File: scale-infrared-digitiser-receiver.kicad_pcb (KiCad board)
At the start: 4 copper layers, 158 x 6 mm, 59 parts, among them IC0 LM324PT, IC1 LM324PT, IC2 LM324PT, IC3 LM324PT

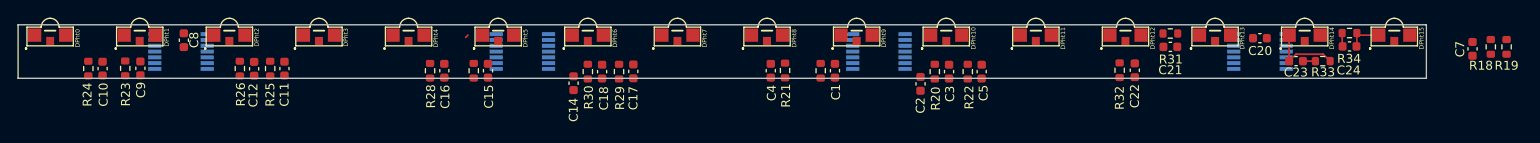
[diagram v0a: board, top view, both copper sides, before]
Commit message: reworking to exclude amplifiers - may need to rollback
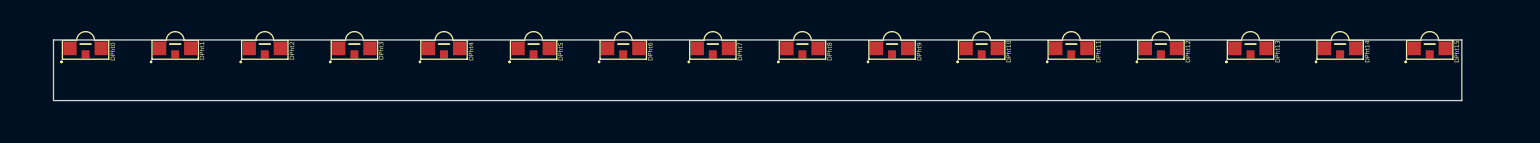
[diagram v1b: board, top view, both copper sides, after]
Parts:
- removed C1, C10, C11, C12, C15, C16, C17, C18, C21, C22, C23, C24, C3, C4, C5, C9: 5.1p, Capacitor_SMD:C_0603_1608Metric
- removed C14, C2, C20, C7, C8: 1u, Capacitor_SMD:C_0603_1608Metric
- removed IC0, IC1, IC2, IC3: LM324PT, Samacsys:SOP65P640X120-14N
- removed R17, R20, R21, R22, R23, R24, R25, R26, R27, R28, R29, R30, R31, R32, R33, R34: 750k, Resistor_SMD:R_0603_1608Metric
- removed R18: 115k, Resistor_SMD:R_0603_1608Metric
- removed R19: 3.57k, Resistor_SMD:R_0603_1608Metric
- moved DPht12 4.25 mm to (194.2, 96.2)
- moved DPht9 4.25 mm to (164.1, 96.2)
- moved DPht1 4.25 mm to (83.7, 96.2)
- moved DPht3 4.25 mm to (103.8, 96.2)
- moved DPht5 4.25 mm to (123.9, 96.2)
- moved DPht0 4.25 mm to (73.6, 96.2)
- moved DPht10 4.25 mm to (174.1, 96.2)
- moved DPht11 4.25 mm to (184.2, 96.2)
- moved DPht13 4.25 mm to (204.3, 96.2)
- moved DPht14 4.25 mm to (214.3, 96.2)
- moved DPht15 4.25 mm to (224.4, 96.2)
- moved DPht2 4.25 mm to (93.7, 96.2)
- moved DPht4 4.25 mm to (113.8, 96.2)
- moved DPht6 4.25 mm to (133.9, 96.2)
- moved DPht7 4.25 mm to (144.0, 96.2)
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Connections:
- DPht0 pad 1: Net-(DPht0-K) -> /PHT_DAT_0
- DPht1 pad 1: Net-(DPht1-K) -> /PHT_DAT_1
- DPht10 pad 1: Net-(DPht10-K) -> /PHT_DAT_10
- DPht11 pad 1: Net-(DPht11-K) -> /PHT_DAT_11
- DPht12 pad 1: Net-(DPht12-K) -> /PHT_DAT_12
- DPht13 pad 1: Net-(DPht13-K) -> /PHT_DAT_13
- DPht14 pad 1: Net-(DPht14-K) -> /PHT_DAT_14
- DPht15 pad 1: Net-(DPht15-K) -> /PHT_DAT_15
- DPht2 pad 1: Net-(DPht2-K) -> /PHT_DAT_2
- DPht3 pad 1: Net-(DPht3-K) -> /PHT_DAT_3
- DPht4 pad 1: Net-(DPht4-K) -> /PHT_DAT_4
- DPht5 pad 1: Net-(DPht5-K) -> /PHT_DAT_5
- DPht6 pad 1: Net-(DPht6-K) -> /PHT_DAT_6
- DPht7 pad 1: Net-(DPht7-K) -> /PHT_DAT_7
- DPht8 pad 1: Net-(DPht8-K) -> /PHT_DAT_8
- DPht9 pad 1: Net-(DPht9-K) -> /PHT_DAT_9
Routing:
- net Net-(DPht14-K): track 8.16 -> 0.00 mm
- net Net-(DPht15-K): track 4.07 -> 0.00 mm
- net /PHT_DAT_15: track 1.52 -> 0.00 mm
- net /PHT_DAT_14: track 1.40 -> 0.00 mm
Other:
- board size 158 x 6 mm -> 158 x 6.8 mm
